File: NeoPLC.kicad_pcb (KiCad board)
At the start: 2 copper layers, 75 x 110 mm, 39 parts, among them J1 Backplane 2x6, J2 DI1-4+COM 3.5mm, J3 DI5-8+COM 3.5mm, J4 SWD, U1 STM32G071CBT6, U2 AP2112K-3.3, U3 ISL3178EIBZ, U4 TLP291-4, U5 TLP291-4, Y1 8MHz

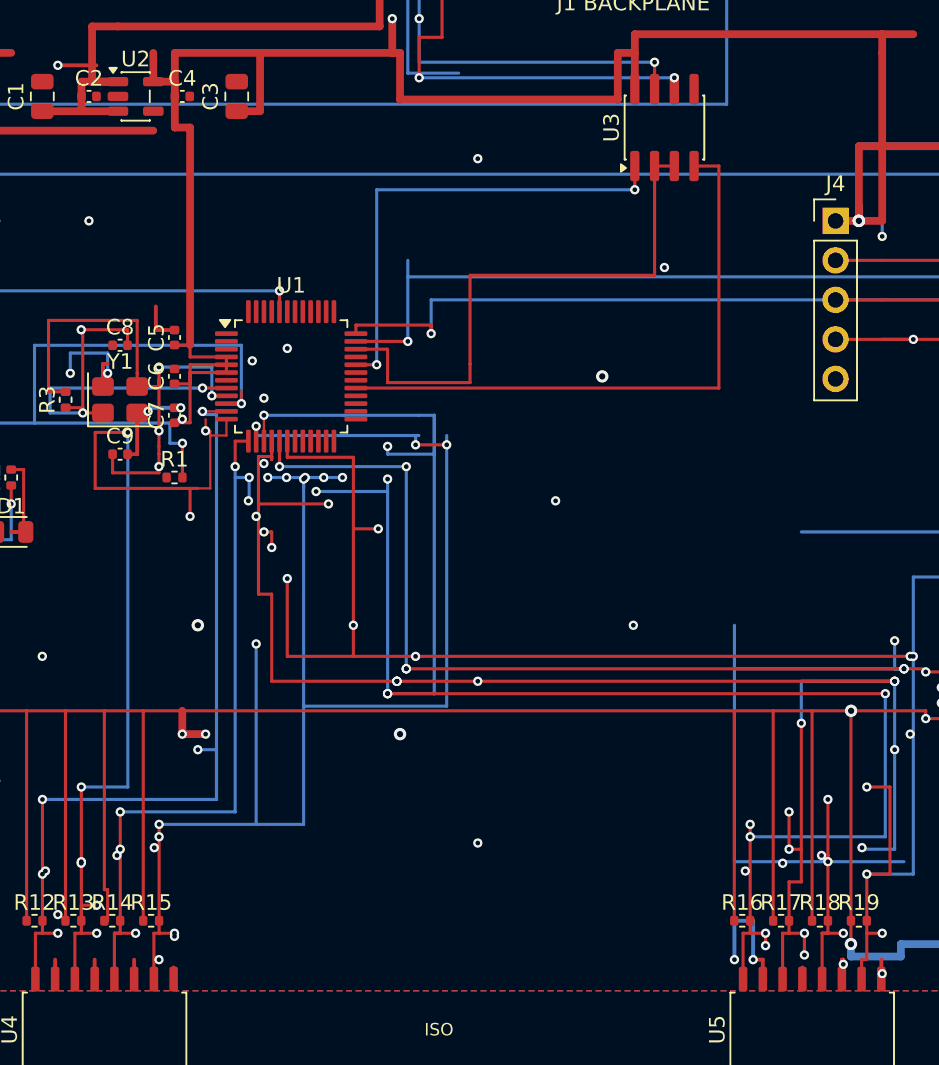
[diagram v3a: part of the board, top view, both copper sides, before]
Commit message: U1 pad7, C2 ve U5 pad13 GND kapandı: DRC 37→33, kısa yok.
Co-authored-by: Cursor <cursoragent@cursor.com>
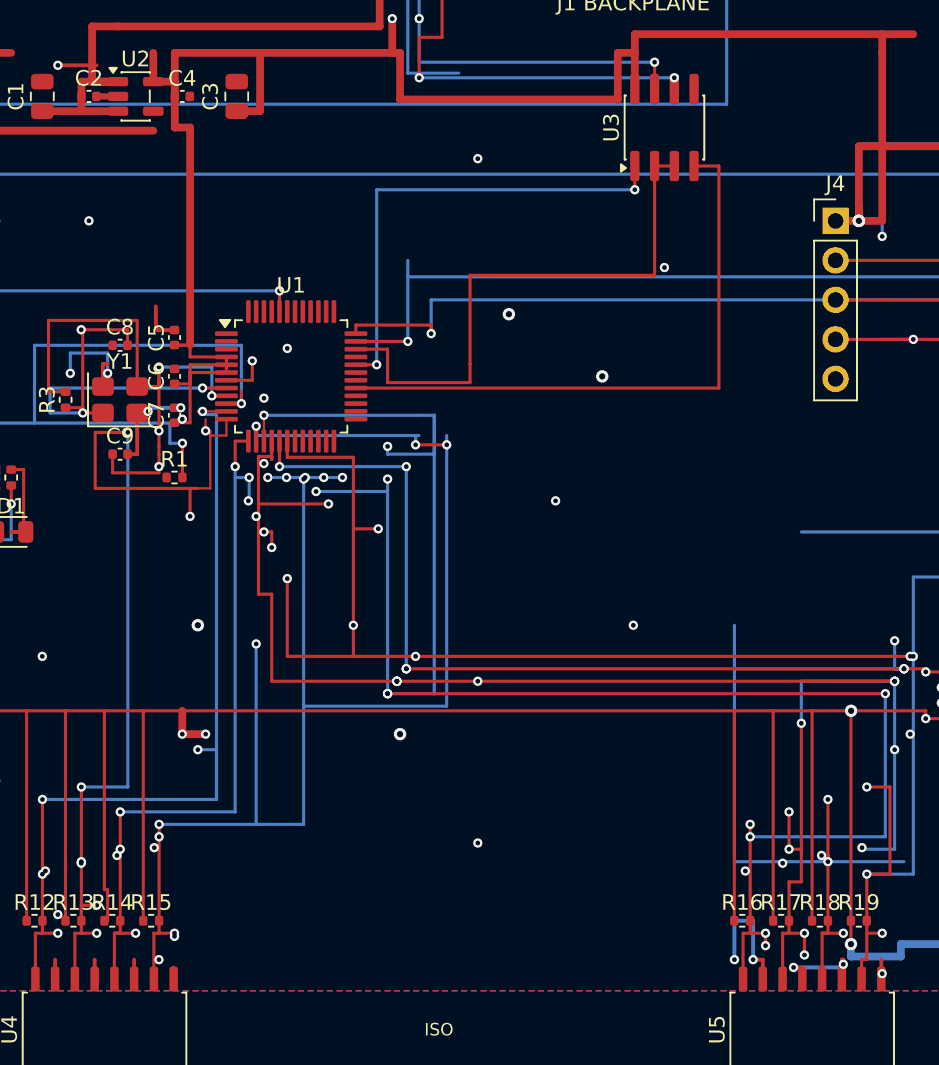
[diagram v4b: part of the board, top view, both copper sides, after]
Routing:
- net GND: track 93.1 -> 101.3 mm, vias 26 -> 28
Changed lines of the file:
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@@
+	)
+	(segment
+		(start 23.8375 32.25)
+		(end 25.5 32.25)
+		(width 0.2)
+		(layer "F.Cu")
+		(net "GND")
 	)
 	(segment
@@
 	)
 	(segment
+		(start 60.865 70)
+		(end 60.3 70)
+		(width 0.25)
+		(layer "F.Cu")
+		(net "GND")
+	)
+	(segment
 		(start 58.325 70.75)
 		(end 58.325 69.5)
 		(width 0.25)
+		(layer "F.Cu")
+		(net "GND")
+	)
+	(segment
+		(start 25.5 32.25)
+		(end 25.5 31)
+		(width 0.2)
 		(layer "F.Cu")
 		(net "GND")
@@
 	)
 	(segment
+		(start 15.48 14)
+		(end 16.8625 14)
+		(width 0.4)
+		(layer "F.Cu")
+		(net "GND")
+	)
+	(segment
 		(start 63.405 70.75)
 		(end 63.405 69.5)
@@
 	)
 	(via
+		(at 42 28)
+		(size 0.8)
+		(drill 0.4)
+		(layers "F.Cu" "B.Cu")
+		(net "GND")
+	)
+	(via
 		(at 18.8 34.25)
 		(size 0.6)
@@
 		(size 0.8)
 		(drill 0.4)
+		(layers "F.Cu" "B.Cu")
+		(net "GND")
+	)
+	(via
+		(at 60.3 70)
+		(size 0.6)
+		(drill 0.3)
 		(layers "F.Cu" "B.Cu")
 		(net "GND")
@@
 	)
 	(segment
+		(start 63.5 70)
+		(end 63.5 69.8)
+		(width 0.25)
+		(layer "B.Cu")
+		(net "GND")
+	)
+	(segment
 		(start 13.8 30.5)
 		(end 16.2 30.5)
@@
 		(layer "B.Cu")
 		(net "GND")
+	)
+	(segment
+		(start 60.3 70)
+		(end 63.5 70)
+		(width 0.25)
+		(layer "B.Cu")
+		(net "GND")

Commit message: C6 ve R1 GND kaçışı: DRC 33→29, kısa yok, açık uç sadece pour adası.
Co-authored-by: Cursor <cursoragent@cursor.com>
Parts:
- moved R1 4.30 mm to (20.5, 42.8)
- moved C6 2.43 mm to (22.2, 30.3)
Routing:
- net GND: track 101.3 -> 119.7 mm, vias 28 -> 32
- net /Node Core/MOD_RST#: track 248.7 -> 255.2 mm, vias 13 -> 14
- net +3V3: track 426.9 -> 425.9 mm
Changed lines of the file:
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@@
 	(footprint "Capacitor_SMD:C_0402_1005Metric"
 		(layer "F.Cu")
-		(at 20.5 32 90)
+		(at 22.2 30.27 90)
 		(property "Reference" "C6"
 			(at 0 -1.16 90)
@@
 	(footprint "Resistor_SMD:R_0402_1005Metric"
 		(layer "F.Cu")
-		(at 20.5 38.5)
+		(at 20.5 42.8)
 		(property "Reference" "R1"
 			(at 0 -1.17 0)
@@
 	)
 	(segment
-		(start 20.5 32.479999)
-		(end 21.5 32.479999)
-		(width 0.2)
-		(layer "F.Cu")
-		(net "+3V3")
-	)
-	(segment
 		(start 15.99 53.5)
 		(end 15.99 65)
@@
 	)
 	(segment
+		(start 20.5 34.02)
+		(end 20.5 33.2)
+		(width 0.2)
+		(layer "F.Cu")
+		(net "GND")
+	)
+	(segment
 		(start 15.365 70.75)
 		(end 15.365 69.5)
@@
 	)
 	(segment
+		(start 22.2 29.79)
+		(end 22.4 29.79)
+		(width 0.2)
+		(layer "F.Cu")
+		(net "GND")
+	)
+	(segment
 		(start 20.5 34.02)
 		(end 20.9 34.02)
@@
 	)
 	(segment
+		(start 22.4 29.79)
+		(end 22.4 28.9)
+		(width 0.2)
+		(layer "F.Cu")
+		(net "GND")
+	)
+	(segment
+		(start 19.99 42.8)
+		(end 19.99 43.3)
+		(width 0.25)
+		(layer "F.Cu")
+		(net "GND")
+	)
+	(segment
 		(start 8.5 42)
 		(end 3.5 42)
@@
 	)
 	(segment
+		(start 19.99 43.3)
+		(end 8.5 43.3)
+		(width 0.25)
+		(layer "F.Cu")
+		(net "GND")
+	)
+	(segment
+		(start 8.5 43.3)
+		(end 8.5 42)
+		(width 0.25)
+		(layer "F.Cu")
+		(net "GND")
+	)
+	(segment
 		(start 8 32)
 		(end 8.5 32)
@@
 	)
 	(via
+		(at 30 62)
+		(size 0.8)
+		(drill 0.4)
+		(layers "F.Cu" "B.Cu")
+		(net "GND")
+	)
+	(via
 		(at 18.8 34.25)
 		(size 0.6)
@@
 	)
 	(via
+		(at 22.4 28.9)
+		(size 0.6)
+		(drill 0.3)
+		(layers "F.Cu" "B.Cu")
+		(net "GND")
+	)
+	(via
 		(at 56.5 69.5)
 		(size 0.6)
@@
 	)
 	(via
+		(at 19.3 29.02)
+		(size 0.6)
+		(drill 0.3)
+		(layers "F.Cu" "B.Cu")
+		(net "GND")
+	)
+	(via
 		(at 52 25)
 		(size 0.6)
@@
 	)
 	(via
+		(at 52 45)
+		(size 0.8)
+		(drill 0.4)
+		(layers "F.Cu" "B.Cu")
+		(net "GND")
+	)
+	(via
 		(at 63.5 69.8)
 		(size 0.6)
@@
 	)
 	(segment
+		(start 22.4 28.9)
+		(end 19.3 28.9)
+		(width 0.25)
+		(layer "B.Cu")
+		(net "GND")
+	)
+	(segment
 		(start 20.9 34.02)
 		(end 18.8 34.02)
@@
 	)
 	(segment
+		(start 19.3 28.9)
+		(end 19.3 29.02)
+		(width 0.25)
+		(layer "B.Cu")
+		(net "GND")
+	)
+	(segment
 		(start 57.7 69.5)
 		(end 57.7 67)
@@
 	)
 	(segment
-		(start 21.01 36.3)
-		(end 21.01 38.5)
+		(start 21.01 42.8)
+		(end 21.01 43.3)
 		(width 0.2)
 		(layer "F.Cu")
@@
 	)
 	(via
+		(at 21.01 43.3)
+		(size 0.6)
+		(drill 0.3)
+		(layers "F.Cu" "B.Cu")
+		(net "/Node Core/MOD_RST#")
+	)
+	(via
 		(at 7 38.5)
 		(size 0.6)
@@
 	)
 	(segment
+		(start 20.4 43.3)
+		(end 20.4 36.3)
+		(width 0.2)
+		(layer "B.Cu")
+		(net "/Node Core/MOD_RST#")
+	)
+	(segment
 		(start 4 31)
 		(end 7 31)
@@
 	)
 	(segment
+		(start 21.01 43.3)
+		(end 20.4 43.3)
+		(width 0.2)
+		(layer "B.Cu")
+		(net "/Node Core/MOD_RST#")
+	)
+	(segment
 		(start 7 23)
 		(end 4 23)
 		(width 0.2)
 		(layer "B.Cu")
+		(net "/Node Core/MOD_RST#")
+	)
+	(segment
+		(start 20.4 36.3)
+		(end 21.01 36.3)
+		(width 0.2)
+		(layer "B.Cu")

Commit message: C7 via, +3V3 omurga ve DI7 kaçışı: DRC 29→26, kısa yok.
Co-authored-by: Cursor <cursoragent@cursor.com>
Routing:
- net GND: track 119.7 -> 139.0 mm, vias 32 -> 36
- net +3V3: track 425.9 -> 427.0 mm, vias 23 -> 24
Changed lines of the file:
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@@
+	)
+	(segment
+		(start 21.5 28.5)
+		(end 21.5 29.98)
+		(width 0.2)
+		(layer "F.Cu")
+		(net "+3V3")
 	)
 	(segment
@@
 	)
 	(segment
-		(start 63.99 68.5)
-		(end 63.99 67)
-		(width 0.2)
-		(layer "F.Cu")
-		(net "+3V3")
-	)
-	(segment
 		(start 56.49 53.5)
 		(end 56.49 67)
@@
 	)
 	(segment
+		(start 21.5 16)
+		(end 21.5 28.5)
+		(width 0.5)
+		(layer "F.Cu")
+		(net "+3V3")
+	)
+	(segment
 		(start 23.8375 31.25)
 		(end 23.8375 31.75)
@@
 	)
 	(segment
-		(start 21.5 29.98)
-		(end 21.5 16)
-		(width 0.5)
-		(layer "F.Cu")
-		(net "+3V3")
-	)
-	(segment
 		(start 70.8 43.7)
 		(end 70.8 41.5)
@@
 	)
 	(via
+		(at 63.99 66.5)
+		(size 0.6)
+		(drill 0.3)
+		(layers "F.Cu" "B.Cu")
+		(net "+3V3")
+	)
+	(via
 		(at 73.5 17.2)
 		(size 0.8)
@@
 	)
 	(segment
+		(start 63.99 68.5)
+		(end 64.3 68.5)
+		(width 0.2)
+		(layer "B.Cu")
+		(net "+3V3")
+	)
+	(segment
 		(start 70.2 53)
 		(end 70.2 58)
@@
 	)
 	(segment
+		(start 64.3 68.5)
+		(end 64.3 66.5)
+		(width 0.2)
+		(layer "B.Cu")
+		(net "+3V3")
+	)
+	(segment
 		(start 73.6 41.5)
 		(end 74 41.5)
@@
 		(end 63.99 69.3)
 		(width 0.5)
+		(layer "B.Cu")
+		(net "+3V3")
+	)
+	(segment
+		(start 64.3 66.5)
+		(end 63.99 66.5)
+		(width 0.2)
 		(layer "B.Cu")
 		(net "+3V3")
@@
 	)
 	(segment
-		(start 20.5 34.02)
-		(end 20.9 34.02)
-		(width 0.25)
-		(layer "F.Cu")
-		(net "GND")
-	)
-	(segment
 		(start 23.8375 32.25)
 		(end 25.5 32.25)
@@
 	)
 	(segment
+		(start 3.5 62)
+		(end 9 62)
+		(width 0.5)
+		(layer "F.Cu")
+		(net "GND")
+	)
+	(segment
 		(start 8.5 11.2)
 		(end 8.5 42)
@@
 	)
 	(segment
+		(start 20.5 34.02)
+		(end 20.25 34.02)
+		(width 0.2)
+		(layer "F.Cu")
+		(net "GND")
+	)
+	(segment
 		(start 8.5 42)
 		(end 3.5 42)
@@
 		(start 3.5 42)
 		(end 3.5 53.5)
+		(width 0.5)
+		(layer "F.Cu")
+		(net "GND")
+	)
+	(segment
+		(start 9 62)
+		(end 9 58)
 		(width 0.5)
 		(layer "F.Cu")
@@
 	)
 	(segment
+		(start 3.5 53.5)
+		(end 3.5 62)
+		(width 0.5)
+		(layer "F.Cu")
+		(net "GND")
+	)
+	(segment
 		(start 19.3 29.02)
 		(end 19.3 27.5)
@@
 	)
 	(via
+		(at 55 58)
+		(size 0.8)
+		(drill 0.4)
+		(layers "F.Cu" "B.Cu")
+		(net "GND")
+	)
+	(via
 		(at 35 55)
 		(size 0.8)
@@
 	)
 	(via
+		(at 45 55)
+		(size 0.8)
+		(drill 0.4)
+		(layers "F.Cu" "B.Cu")
+		(net "GND")
+	)
+	(via
 		(at 8 48)
 		(size 0.8)
@@
 	)
 	(via
-		(at 20.9 34.02)
-		(size 0.6)
-		(drill 0.3)
-		(layers "F.Cu" "B.Cu")
-		(net "GND")
-	)
-	(via
 		(at 15 22)
 		(size 0.6)
@@
 	)
 	(via
+		(at 42 60)
+		(size 0.8)
+		(drill 0.4)
+		(layers "F.Cu" "B.Cu")
+		(net "GND")
+	)
+	(via
 		(at 22.4 28.9)
 		(size 0.6)
@@
 	)
 	(via
+		(at 20.25 34.02)
+		(size 0.6)
+		(drill 0.3)
+		(layers "F.Cu" "B.Cu")
+		(net "GND")
+	)
+	(via
 		(at 66 70.4)
 		(size 0.6)
@@
 		(size 0.6)
 		(drill 0.3)
+		(layers "F.Cu" "B.Cu")
+		(net "GND")
+	)
+	(via
+		(at 60 48)
+		(size 0.8)
+		(drill 0.4)
 		(layers "F.Cu" "B.Cu")
 		(net "GND")
@@
 		(width 0.25)
 		(layer "B.Cu")
+		(net "GND")
+	)
+	(segment
+		(start 20.25 34.02)
+		(end 18.8 34.02)
+		(width 0.25)
+		(layer "B.Cu")

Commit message: DI5 yanındaki GND via çıktı: DRC 26→25, kısa yok.
Co-authored-by: Cursor <cursoragent@cursor.com>
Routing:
- net GND: track 139.0 -> 135.3 mm, vias 36 -> 35
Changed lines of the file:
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@@
-	)
-	(via
-		(at 56.5 69.5)
-		(size 0.6)
-		(drill 0.3)
-		(layers "F.Cu" "B.Cu")
-		(net "GND")
 	)
 	(via
@@
 	)
 	(segment
-		(start 57.7 67)
-		(end 56.5 67)
-		(width 0.25)
-		(layer "B.Cu")
-		(net "GND")
-	)
-	(segment
 		(start 63.5 70)
 		(end 63.5 69.8)
@@
 		(width 0.25)
 		(layer "B.Cu")
-		(net "GND")
-	)
-	(segment
-		(start 56.5 67)
-		(end 56.5 69.5)
-		(width 0.25)
-		(layer "B.Cu")

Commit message: U4 GND adaları via ile kapandı: DRC açık uç 3→0.
Co-authored-by: Cursor <cursoragent@cursor.com>
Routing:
- net GND: vias 35 -> 38
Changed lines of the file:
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@@
+	)
+	(via
+		(at 15.365 69.5)
+		(size 0.6)
+		(drill 0.3)
+		(layers "F.Cu" "B.Cu")
+		(net "GND")
 	)
 	(via
@@
 		(size 0.6)
 		(drill 0.3)
+		(layers "F.Cu" "B.Cu")
+		(net "GND")
+	)
+	(via
+		(at 17.905 69.5)
+		(size 0.6)
+		(drill 0.3)
+		(layers "F.Cu" "B.Cu")
+		(net "GND")
+	)
+	(via
+		(at 12.825 69.5)
+		(size 0.6)
+		(drill 0.3)
